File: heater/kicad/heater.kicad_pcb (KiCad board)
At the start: 2 copper layers, 90 x 88.4 mm, 80 parts, among them J1 Conn_01x02_Pin, J2 Conn_01x02_Pin, J3 pcie_98, U1 OPA863SIDBVR, U11 ESD5344D-TP, U12 ESD5344D-TP, U13 XC6206P332MR, U15 TPS7A2025PDBVR, U2 D050505T-1WR4, U3 LTC1968, U4 LTC1968, U5 TPS72325DBVR, U8 ADS1115IDGS, U9 ISO1541

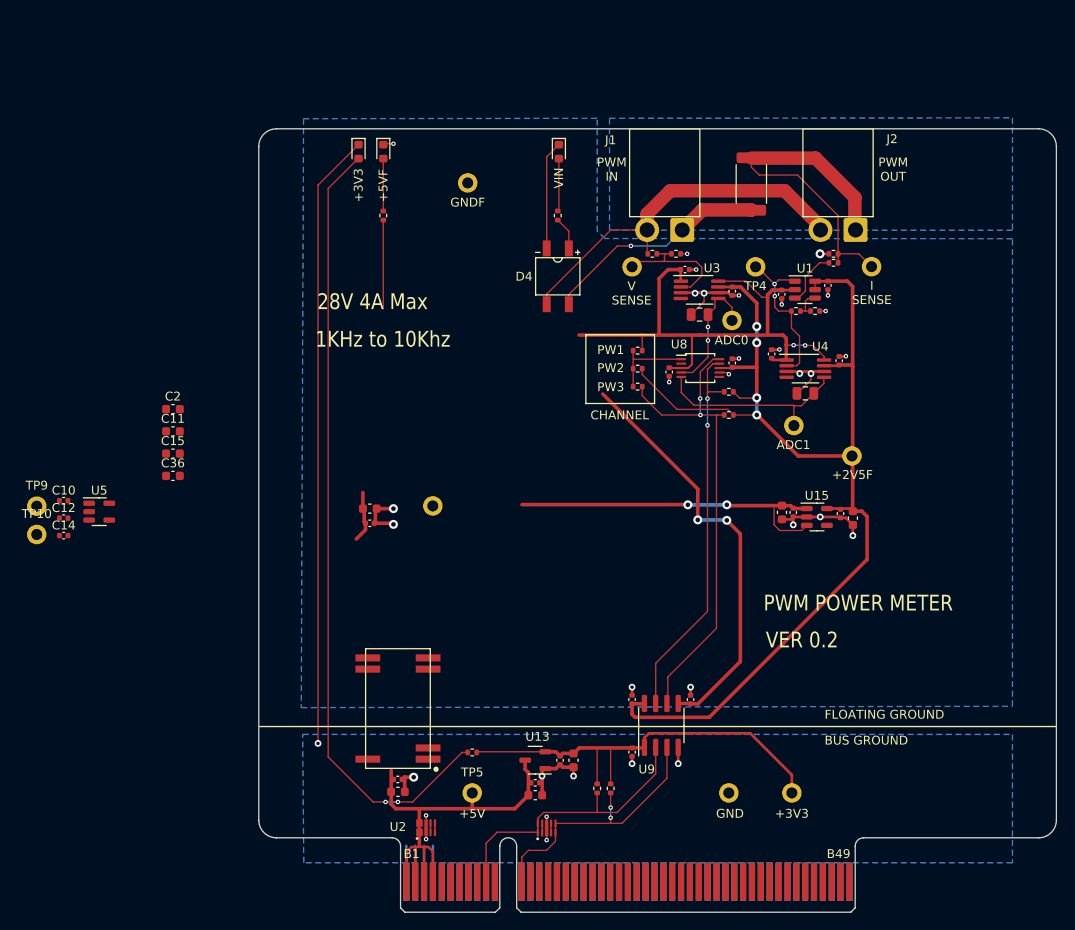
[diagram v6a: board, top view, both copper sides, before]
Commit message: Cleaned up the heater layout.
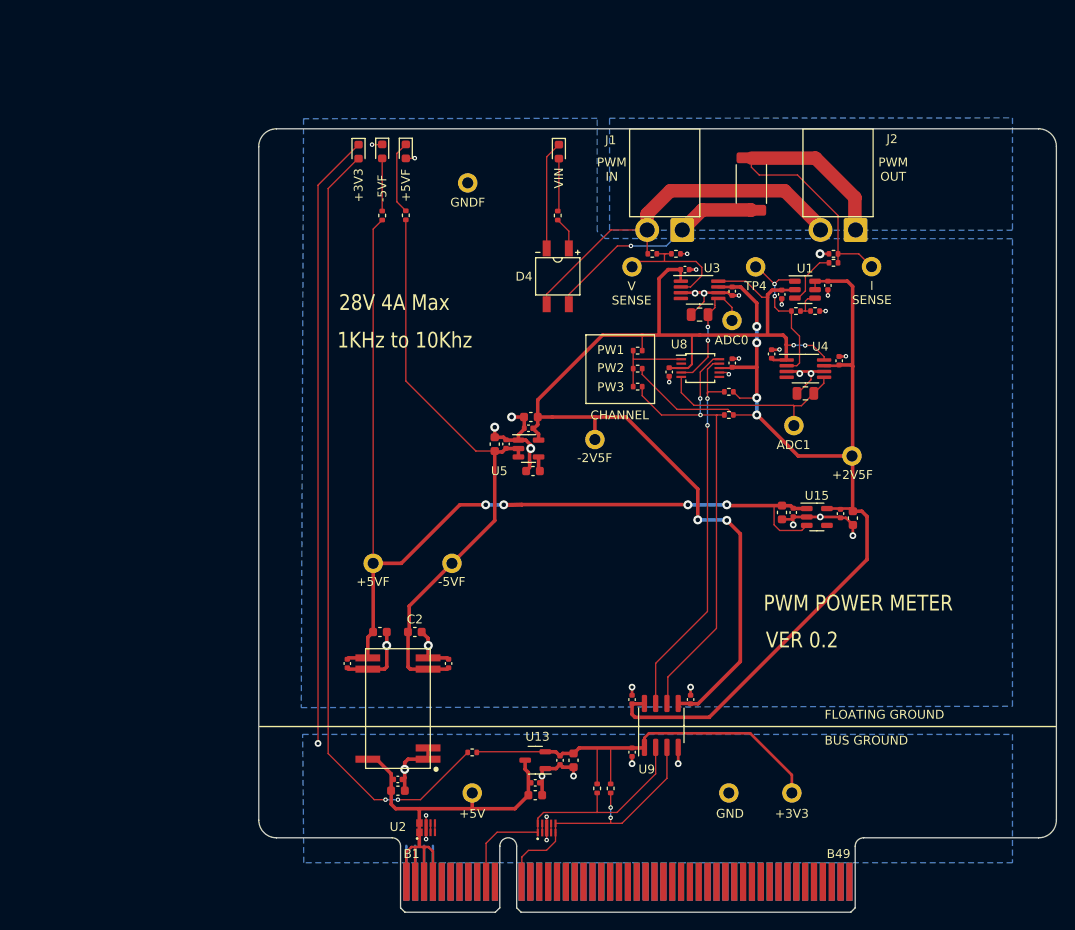
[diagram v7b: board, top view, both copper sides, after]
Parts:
- added D2: GRN, LED_SMD:LED_0603_1608Metric, F.Cu at (-14.2, -85.9)
- added R7: 5K1, Resistor_SMD:R_0402_1005Metric, F.Cu at (-14.2, -78.6)
- moved TP10 63.9 mm to (9.78, -53.3)
- moved C14 53.8 mm to (2.29, -54.6)
- moved C12 50.6 mm to (-0.25, -52.8), turned to -90 degrees
- moved U5 49.0 mm to (2.29, -52.3)
- moved TP9 47.3 mm to (-6.35, -39.4)
- moved C10 47.2 mm to (-6.73, -28.1), turned to 90 degrees
- moved C36 40.6 mm to (2.79, -49.8)
- moved C15 40.6 mm to (2.55, -55.9)
- moved C2 37.1 mm to (-10.5, -31.6)
- moved C11 36.3 mm to (-1.52, -52.8), turned to -90 degrees
- moved C17 16.0 mm to (-18.2, -28.1), turned to 90 degrees
- moved C16 14.0 mm to (-14.5, -31.6)
- moved TP11 9.34 mm to (-15.2, -39.4)
- moved D1 2.54 mm to (-11.6, -85.9)
- moved R5 2.54 mm to (-11.6, -78.6)
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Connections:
- D1 pad 1: GNDF -> Net-(D1-K)
- D1 pad 2: Net-(D1-A) -> GNDF
- R5 pad 1: +5VF -> -5VF
- R5 pad 2: Net-(D1-A) -> Net-(D1-K)
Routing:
- net -5VF: track 0.00 -> 68.5 mm
- net +5VF: track 53.9 -> 112.1 mm, vias 2 -> 4
- net GNDF: track 45.3 -> 67.9 mm, vias 24 -> 28
- net -2V5F: track 113.4 -> 135.0 mm
- net Net-(D1-K): track 0.00 -> 8.33 mm
- net Net-(D2-A): track 0.00 -> 5.94 mm
- net Net-(D1-A): track 5.92 -> 0.00 mm
- net GND: track 104.2 -> 108.5 mm
- net +5V: track 48.6 -> 51.5 mm
- net Net-(U5-NR): track 0.00 -> 1.65 mm
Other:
- board text added: "-2V5F"
- board text added: "-5VF"

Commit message: Updated the heater schematic.
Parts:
- removed U4: LTC1968, Package_SO:MSOP-8_3x3mm_P0.65mm
- added U6: LTC1966, Package_SO:MSOP-8_3x3mm_P0.65mm, F.Cu at (33.5, -61.3)
- U3: value LTC1968 -> LTC1966
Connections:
- U3 pad 4: unconnected-(U3-NC-Pad4) -> -2V5F
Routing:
- net -2V5F: track 135.0 -> 142.7 mm
